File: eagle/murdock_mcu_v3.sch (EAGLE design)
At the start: 32 parts, among them IC1 MPU-9150, IC2 LT1763CS8-3.3, IC3 STM32F4XX_64, IC4 BMP085, Q2 PFET, U1 USD-SOCKETNEW, X2 MURDOCK_STACK

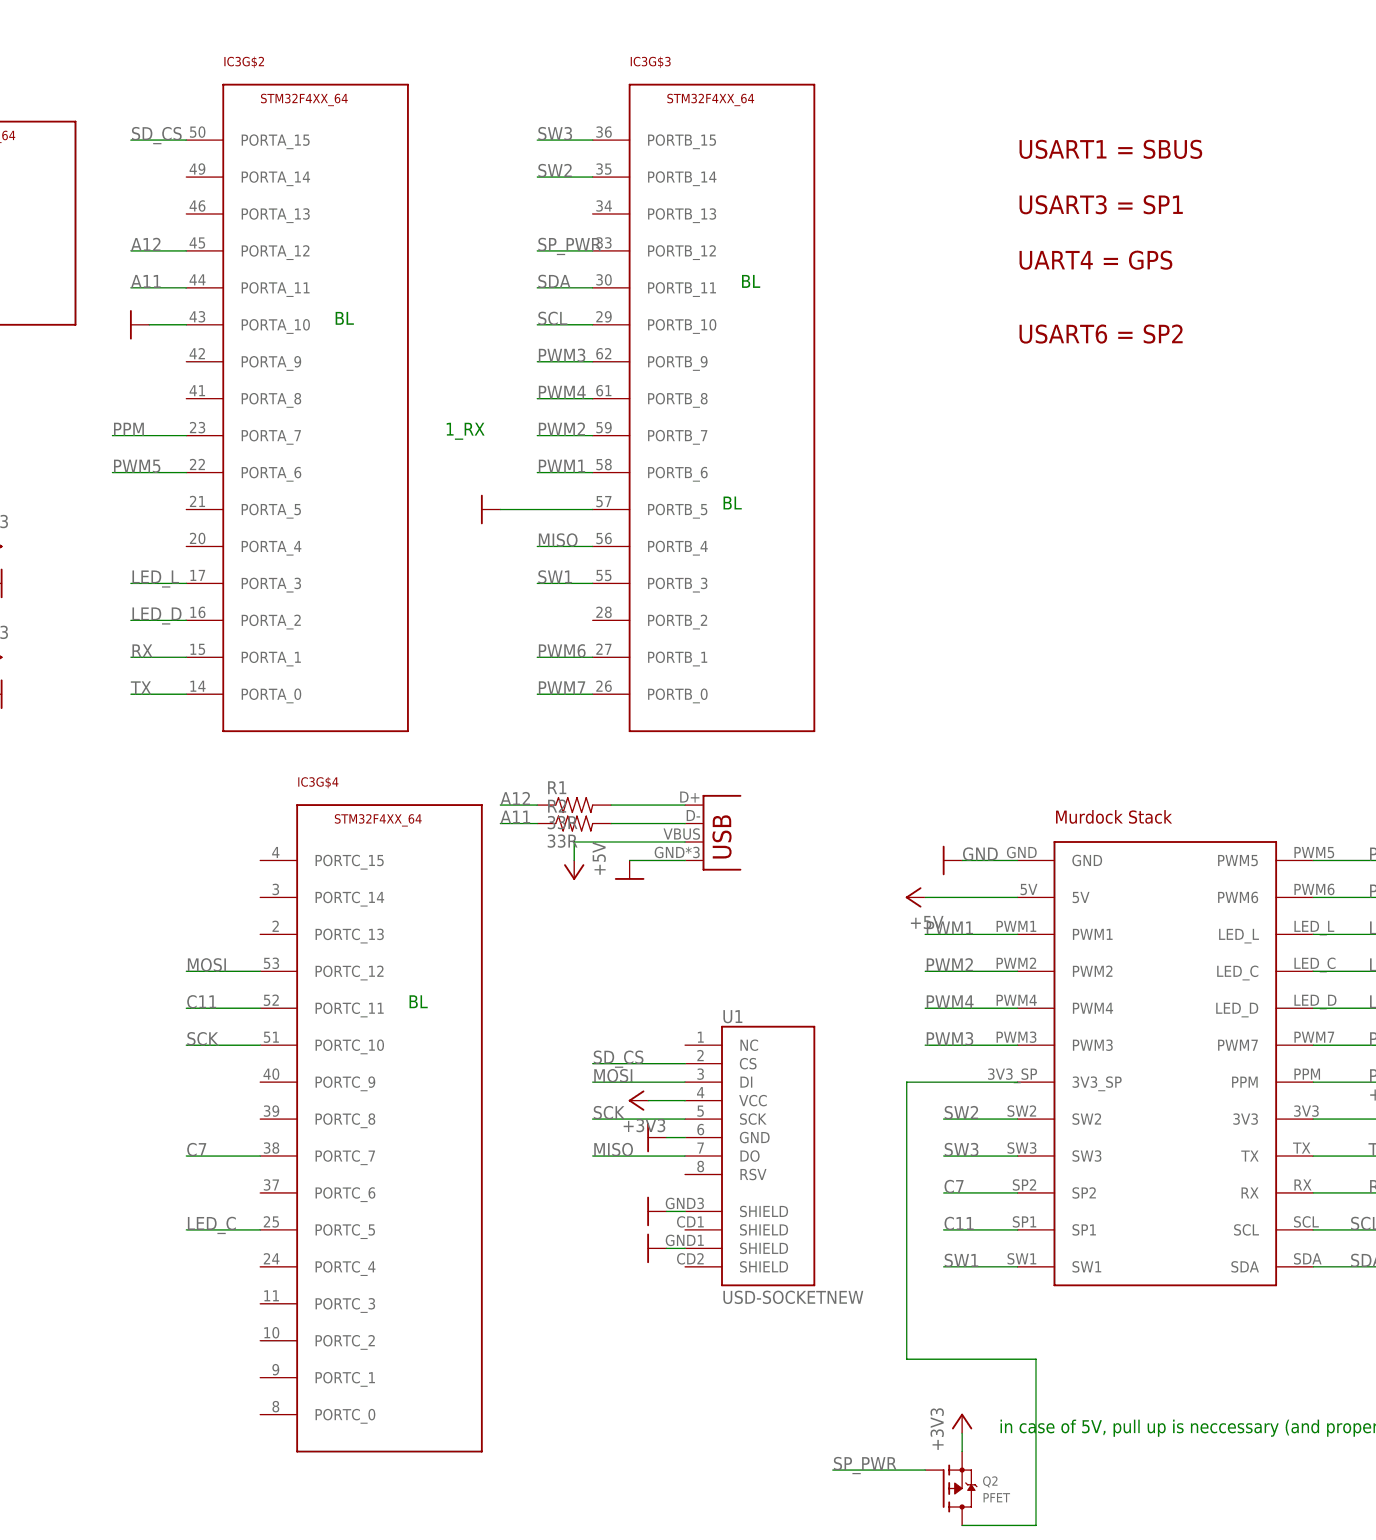
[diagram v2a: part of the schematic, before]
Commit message: pwm/sbus to new pin @usart2 & led_l moved
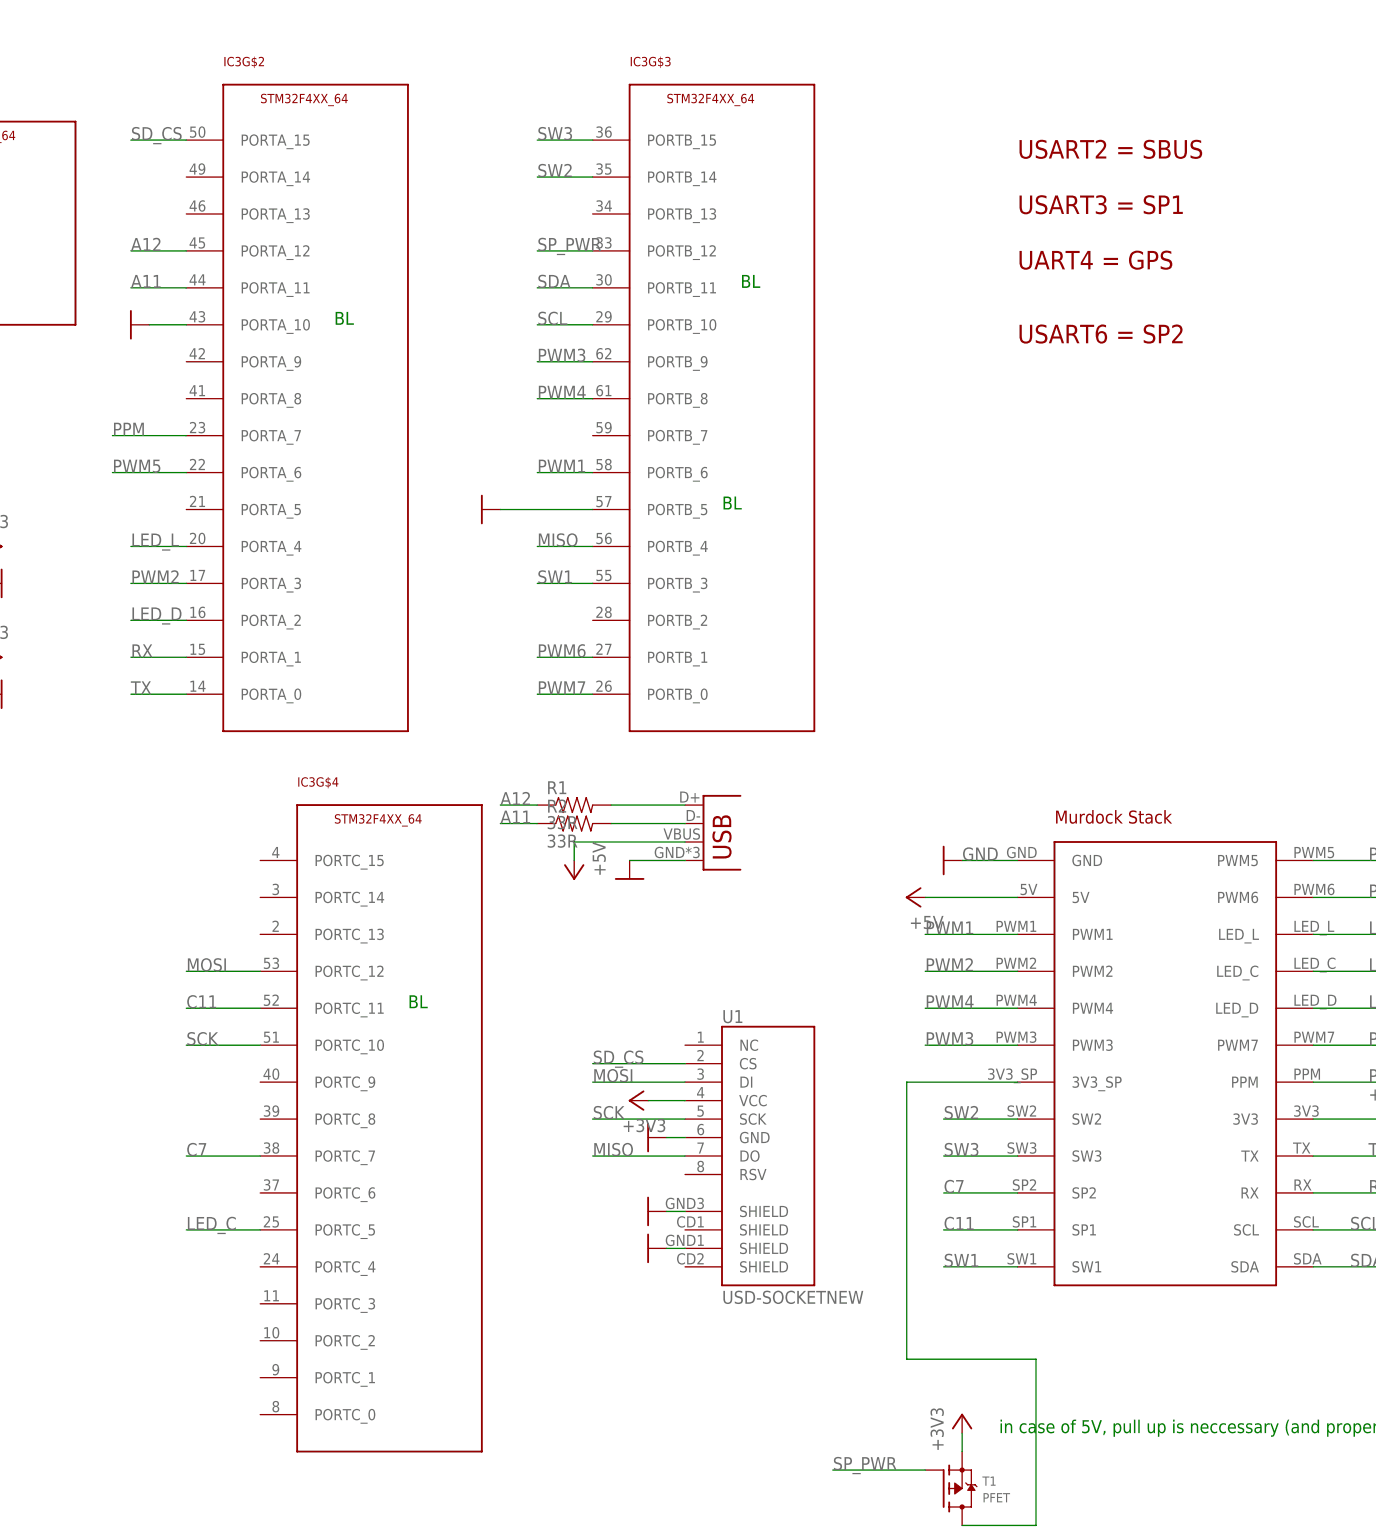
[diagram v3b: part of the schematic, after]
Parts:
- renumbered Q2 to T1
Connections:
- net LED_L: now also IC3G$2.PORTA_4; no longer IC3G$2.PORTA_3
- net PWM2: now also IC3G$2.PORTA_3; no longer IC3G$3.PORTB_7
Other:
- note added: "USART2 = SBUS"
- note removed: "1_RX"
- note removed: "USART1 = SBUS"
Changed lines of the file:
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@@
 <part name="GND15" library="SparkFun-Aesthetics" deviceset="GND" device=""/>
 <part name="P+2" library="supply1" deviceset="+5V" device=""/>
-<part name="Q2" library="microbuilder" deviceset="MOSFET-P" device="" value="PFET"/>
+<part name="T1" library="microbuilder" deviceset="MOSFET-P" device="" value="PFET"/>
 <part name="+3V7" library="supply1" deviceset="+3V3" device=""/>
 <part name="GND17" library="supply1" deviceset="GND" device=""/>
@@
 <text x="-93.98" y="60.96" size="1.778" layer="91">defined value on the bootloader pins</text>
 <text x="96.52" y="149.86" size="2.54" layer="94">UART4 = GPS</text>
-<text x="96.52" y="165.1" size="2.54" layer="94">USART1 = SBUS</text>
+<text x="96.52" y="165.1" size="2.54" layer="94">USART2 = SBUS</text>
 <text x="96.52" y="139.7" size="2.54" layer="94">USART6 = SP2</text>
 <text x="96.52" y="157.48" size="2.54" layer="94">USART3 = SP1</text>
-<text x="17.78" y="127" size="1.778" layer="91">1_RX</text>
 <text x="93.98" y="-10.16" size="1.778" layer="91">in case of 5V, pull up is neccessary (and proper pin configuraiotn)</text>
 <text x="2.54" y="142.24" size="1.778" layer="91">BL</text>
@@
 <instance part="GND15" gate="1" x="22.86" y="116.84" smashed="yes" rot="R270"/>
 <instance part="P+2" gate="1" x="35.56" y="66.04" rot="R180"/>
-<instance part="Q2" gate="G$1" x="88.9" y="-17.78"/>
+<instance part="T1" gate="G$1" x="88.9" y="-17.78"/>
 <instance part="+3V7" gate="G$1" x="88.9" y="-7.62"/>
 <instance part="GND17" gate="1" x="185.42" y="147.32" rot="R270"/>
@@
 <segment>
 <pinref part="+3V7" gate="G$1" pin="+3V3"/>
-<pinref part="Q2" gate="G$1" pin="S"/>
+<pinref part="T1" gate="G$1" pin="S"/>
 <wire x1="88.9" y1="-12.7" x2="88.9" y2="-10.16" width="0.1524" layer="91"/>
 </segment>
@@
 </segment>
 <segment>
-<pinref part="IC3" gate="G$3" pin="PORTB_7"/>
-<wire x1="38.1" y1="127" x2="30.48" y2="127" width="0.1524" layer="91"/>
-<label x="30.48" y="127" size="1.778" layer="95"/>
+<pinref part="IC3" gate="G$2" pin="PORTA_3"/>
+<wire x1="-17.78" y1="106.68" x2="-25.4" y2="106.68" width="0.1524" layer="91"/>
+<label x="-25.4" y="106.68" size="1.778" layer="95"/>
 </segment>
 </net>
@@
 <net name="N$8" class="0">
 <segment>
-<pinref part="Q2" gate="G$1" pin="D"/>
+<pinref part="T1" gate="G$1" pin="D"/>
 <wire x1="88.9" y1="-22.86" x2="99.06" y2="-22.86" width="0.1524" layer="91"/>
 <wire x1="99.06" y1="-22.86" x2="99.06" y2="0" width="0.1524" layer="91"/>
@@
 <net name="SP_PWR" class="0">
 <segment>
-<pinref part="Q2" gate="G$1" pin="G"/>
+<pinref part="T1" gate="G$1" pin="G"/>
 <wire x1="83.82" y1="-15.24" x2="71.12" y2="-15.24" width="0.1524" layer="91"/>
 <label x="71.12" y="-15.24" size="1.778" layer="95"/>
@@
 </segment>
 <segment>
-<pinref part="IC3" gate="G$2" pin="PORTA_3"/>
-<wire x1="-17.78" y1="106.68" x2="-25.4" y2="106.68" width="0.1524" layer="91"/>
-<label x="-25.4" y="106.68" size="1.778" layer="95"/>
-</segment>
-</net>
+<pinref part="IC3" gate="G$2" pin="PORTA_4"/>
+<wire x1="-17.78" y1="111.76" x2="-25.4" y2="111.76" width="0.1524" layer="91"/>
+<label x="-25.4" y="111.76" size="1.778" layer="95"/>
+</segment>
+</net>

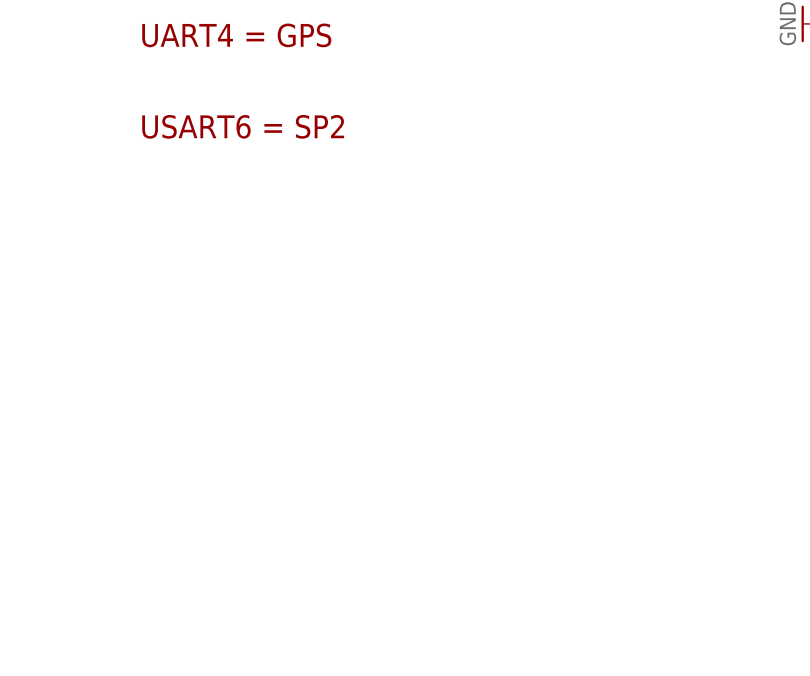
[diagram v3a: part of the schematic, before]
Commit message: added eeprom
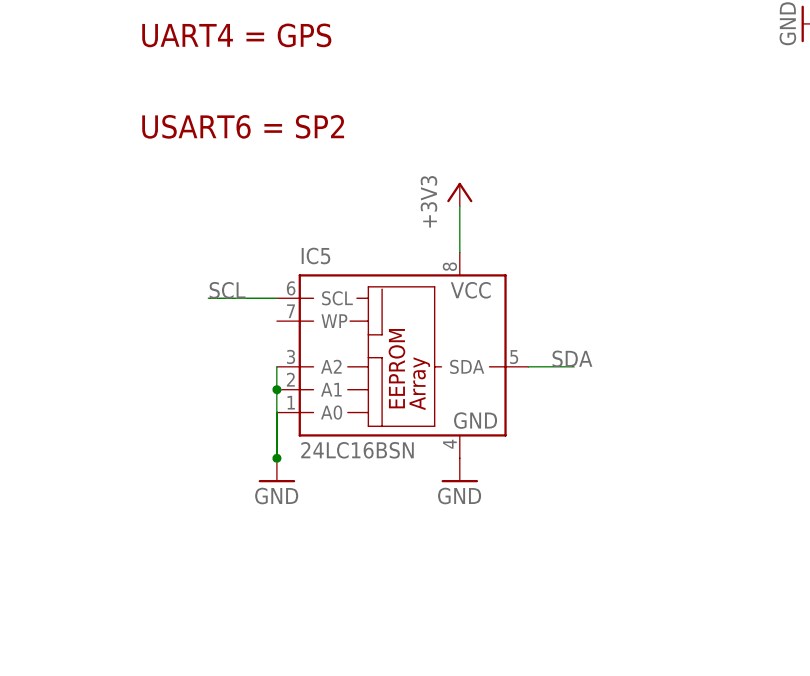
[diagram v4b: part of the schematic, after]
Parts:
- added IC5: 24LC16BSN, microchip:24LC16BSN
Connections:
- net +3V3: now also IC5.VCC
- net GND: now also IC5.A0, IC5.A1, IC5.A2, IC5.GND
- net SCL: now also IC5.SCL
- net SDA: now also IC5.SDA
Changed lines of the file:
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@@
 <part name="R6" library="SparkFun" deviceset="RESISTOR" device="0402-RES" value="15k"/>
 <part name="GND16" library="SparkFun-Aesthetics" deviceset="GND" device=""/>
+<part name="GND28" library="supply1" deviceset="GND" device=""/>
+<part name="IC5" library="microchip" deviceset="24*" device="SN" technology="LC16B"/>
+<part name="+3V13" library="supply1" deviceset="+3V3" device=""/>
+<part name="GND29" library="supply1" deviceset="GND" device=""/>
 </parts>
 <sheets>
@@
 <instance part="R6" gate="G$1" x="-86.36" y="111.76" rot="R90"/>
 <instance part="GND16" gate="1" x="-86.36" y="104.14" smashed="yes"/>
+<instance part="GND28" gate="1" x="132.08" y="101.6"/>
+<instance part="IC5" gate="G$1" x="124.46" y="114.3"/>
+<instance part="+3V13" gate="G$1" x="132.08" y="134.62"/>
+<instance part="GND29" gate="1" x="111.76" y="101.6"/>
 </instances>
 <busses>
@@
 <pinref part="GND16" gate="1" pin="GND"/>
 </segment>
+<segment>
+<pinref part="IC5" gate="G$1" pin="GND"/>
+<pinref part="GND28" gate="1" pin="GND"/>
+</segment>
+<segment>
+<pinref part="IC5" gate="G$1" pin="A2"/>
+<pinref part="IC5" gate="G$1" pin="A1"/>
+<wire x1="111.76" y1="114.3" x2="111.76" y2="111.76" width="0.1524" layer="91"/>
+<pinref part="IC5" gate="G$1" pin="A0"/>
+<wire x1="111.76" y1="111.76" x2="111.76" y2="104.14" width="0.1524" layer="91"/>
+<junction x="111.76" y="111.76"/>
+<pinref part="GND29" gate="1" pin="GND"/>
+<junction x="111.76" y="104.14"/>
+<wire x1="111.76" y1="104.14" x2="111.76" y2="109.22" width="0.1524" layer="91"/>
+</segment>
 </net>
 <net name="+3V3" class="0">
@@
 <pinref part="+3V12" gate="G$1" pin="+3V3"/>
 </segment>
+<segment>
+<pinref part="IC5" gate="G$1" pin="VCC"/>
+<pinref part="+3V13" gate="G$1" pin="+3V3"/>
+<wire x1="132.08" y1="132.08" x2="132.08" y2="127" width="0.1524" layer="91"/>
+</segment>
 </net>
 <net name="+5V" class="0">
@@
 <wire x1="309.88" y1="160.02" x2="292.1" y2="160.02" width="0.1524" layer="91"/>
 </segment>
+<segment>
+<pinref part="IC5" gate="G$1" pin="SDA"/>
+<wire x1="139.7" y1="114.3" x2="144.78" y2="114.3" width="0.1524" layer="91"/>
+<label x="142.24" y="114.3" size="1.778" layer="95"/>
+</segment>
 </net>
 <net name="SCL" class="0">
@@
 <wire x1="304.8" y1="162.56" x2="309.88" y2="162.56" width="0.1524" layer="91"/>
 </segment>
-</net>
+<segment>
+<pinref part="IC5" gate="G$1" pin="SCL"/>
+<wire x1="104.14" y1="121.92" x2="111.76" y2="121.92" width="0.1524" layer="91"/>
+<label x="104.14" y="121.92" size="1.778" layer="95"/>
+</segment>
+</net>

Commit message: usb fix
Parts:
- added R7: 15k, SparkFun-Resistors:RESISTOR0402-RES
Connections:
- net +3V3: now also R7.1
- net +5V: now also IC3G$2.PORTA_9
- net SP_PWR: now also R7.2
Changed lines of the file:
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@@
 <part name="+3V13" library="supply1" deviceset="+3V3" device=""/>
 <part name="GND29" library="supply1" deviceset="GND" device=""/>
+<part name="R7" library="SparkFun-Resistors" deviceset="RESISTOR" device="0402-RES" value="15k"/>
+<part name="P+4" library="supply1" deviceset="+5V" device=""/>
 </parts>
 <sheets>
@@
 <instance part="+3V13" gate="G$1" x="132.08" y="134.62"/>
 <instance part="GND29" gate="1" x="111.76" y="101.6"/>
+<instance part="R7" gate="G$1" x="78.74" y="-10.16" rot="R180"/>
+<instance part="P+4" gate="1" x="-30.48" y="137.16" rot="R90"/>
 </instances>
 <busses>
@@
 <pinref part="T1" gate="G$1" pin="S"/>
 <wire x1="88.9" y1="-12.7" x2="88.9" y2="-10.16" width="0.1524" layer="91"/>
+<pinref part="R7" gate="G$1" pin="1"/>
+<wire x1="83.82" y1="-10.16" x2="88.9" y2="-10.16" width="0.1524" layer="91"/>
+<junction x="88.9" y="-10.16"/>
 </segment>
 <segment>
@@
 <wire x1="35.56" y1="71.12" x2="50.8" y2="71.12" width="0.1524" layer="91"/>
 <pinref part="JP1" gate="G$1" pin="VBUS"/>
+<wire x1="35.56" y1="71.12" x2="25.4" y2="71.12" width="0.1524" layer="91"/>
+<junction x="35.56" y="71.12"/>
+<label x="25.4" y="71.12" size="1.778" layer="95"/>
+</segment>
+<segment>
+<pinref part="IC3" gate="G$2" pin="PORTA_9"/>
+<wire x1="-17.78" y1="137.16" x2="-27.94" y2="137.16" width="0.1524" layer="91"/>
+<label x="-27.94" y="137.16" size="1.778" layer="95"/>
+<pinref part="P+4" gate="1" pin="+5V"/>
 </segment>
 </net>
@@
 <segment>
 <pinref part="T1" gate="G$1" pin="G"/>
-<wire x1="83.82" y1="-15.24" x2="71.12" y2="-15.24" width="0.1524" layer="91"/>
-<label x="71.12" y="-15.24" size="1.778" layer="95"/>
-</segment>
-<segment>
+<wire x1="83.82" y1="-15.24" x2="73.66" y2="-15.24" width="0.1524" layer="91"/>
+<label x="60.96" y="-15.24" size="1.778" layer="95"/>
+<pinref part="R7" gate="G$1" pin="2"/>
+<wire x1="73.66" y1="-15.24" x2="60.96" y2="-15.24" width="0.1524" layer="91"/>
+<wire x1="73.66" y1="-10.16" x2="73.66" y2="-15.24" width="0.1524" layer="91"/>
+<junction x="73.66" y="-15.24"/>
+</segment>
+<segment>

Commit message: merge
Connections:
- new net SCL2: IC3G$2.PORTA_8, X2.SCL
- new net SDA2: IC3G$4.PORTC_9, X2.SDA
- net SCL: no longer X2.SCL
- net SDA: no longer X2.SDA
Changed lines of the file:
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@@
 <?xml version="1.0" encoding="utf-8"?>
 <!DOCTYPE eagle SYSTEM "eagle.dtd">
-<eagle version="6.4">
+<eagle version="6.3">
 <drawing>
 <settings>
@@
 <net name="SDA" class="0">
 <segment>
-<pinref part="X2" gate="G$1" pin="SDA"/>
-<wire x1="137.16" y1="12.7" x2="147.32" y2="12.7" width="0.1524" layer="91"/>
-<label x="142.24" y="12.7" size="1.778" layer="95"/>
-</segment>
-<segment>
 <pinref part="IC3" gate="G$3" pin="PORTB_11"/>
 <wire x1="38.1" y1="147.32" x2="30.48" y2="147.32" width="0.1524" layer="91"/>
@@
 </net>
 <net name="SCL" class="0">
-<segment>
-<pinref part="X2" gate="G$1" pin="SCL"/>
-<wire x1="137.16" y1="17.78" x2="147.32" y2="17.78" width="0.1524" layer="91"/>
-<label x="142.24" y="17.78" size="1.778" layer="95"/>
-</segment>
 <segment>
 <pinref part="IC3" gate="G$3" pin="PORTB_10"/>
@@
 </segment>
 </net>
+<net name="SCL2" class="0">
+<segment>
+<pinref part="IC3" gate="G$2" pin="PORTA_8"/>
+<wire x1="-17.78" y1="132.08" x2="-25.4" y2="132.08" width="0.1524" layer="91"/>
+<label x="-25.4" y="132.08" size="1.778" layer="95"/>
+</segment>
+<segment>
+<pinref part="X2" gate="G$1" pin="SCL"/>
+<wire x1="137.16" y1="17.78" x2="147.32" y2="17.78" width="0.1524" layer="91"/>
+<label x="142.24" y="17.78" size="1.778" layer="95"/>
+</segment>
+</net>
+<net name="SDA2" class="0">
+<segment>
+<pinref part="IC3" gate="G$4" pin="PORTC_9"/>
+<wire x1="-7.62" y1="38.1" x2="-15.24" y2="38.1" width="0.1524" layer="91"/>
+<label x="-15.24" y="38.1" size="1.778" layer="95"/>
+</segment>
+<segment>
+<pinref part="X2" gate="G$1" pin="SDA"/>
+<wire x1="137.16" y1="12.7" x2="147.32" y2="12.7" width="0.1524" layer="91"/>
+<label x="142.24" y="12.7" size="1.778" layer="95"/>
+</segment>
+</net>
